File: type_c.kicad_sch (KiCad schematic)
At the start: 14 parts, among them U12 FUSB302B, U14 DPO2036

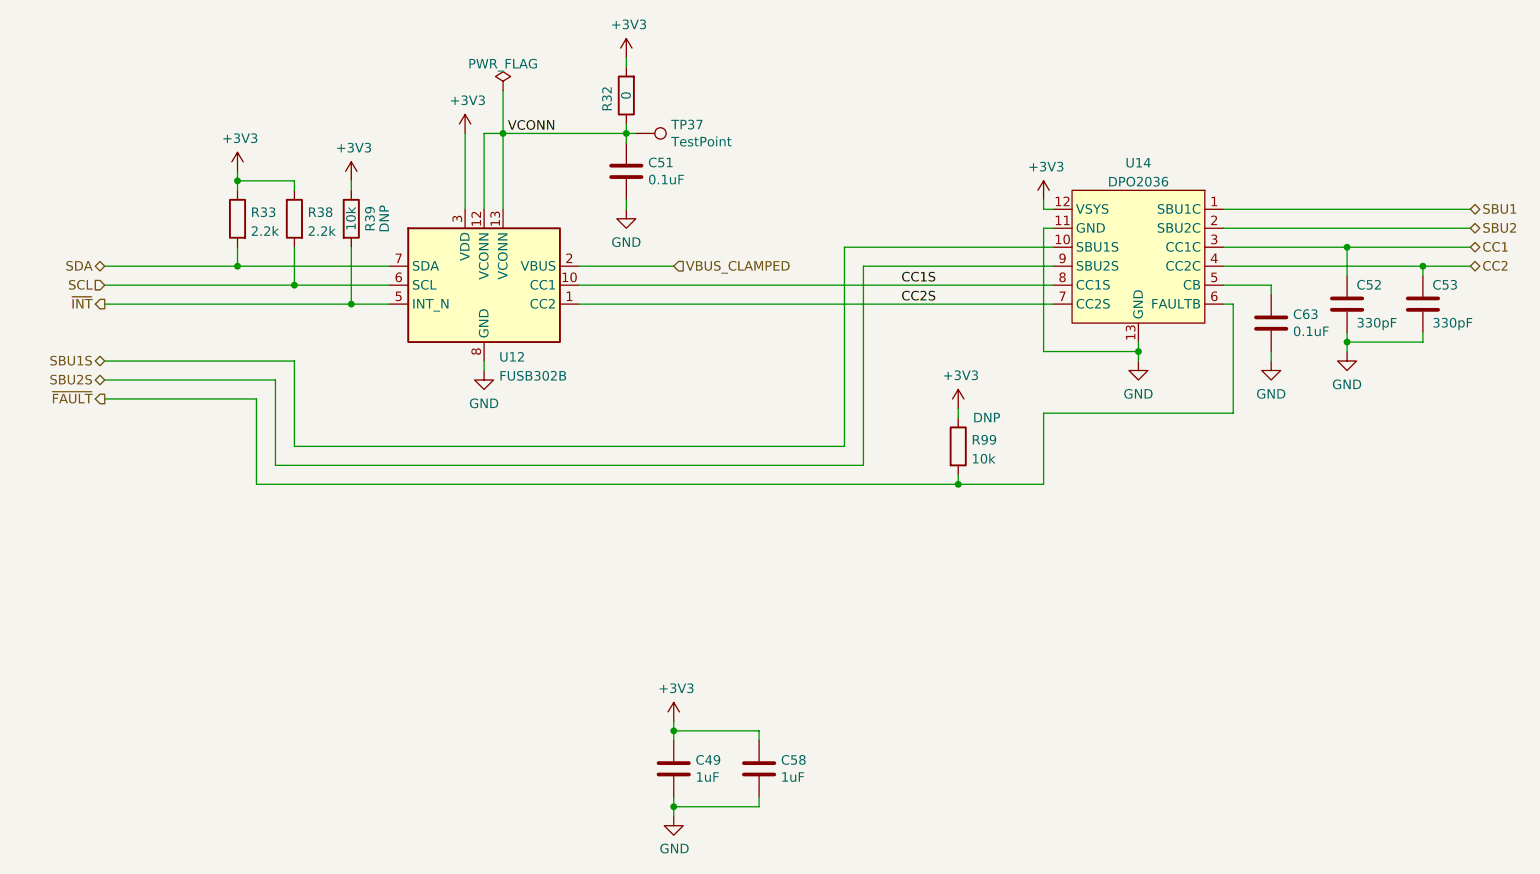
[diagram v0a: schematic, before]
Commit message: Upgrade to KiCad 7
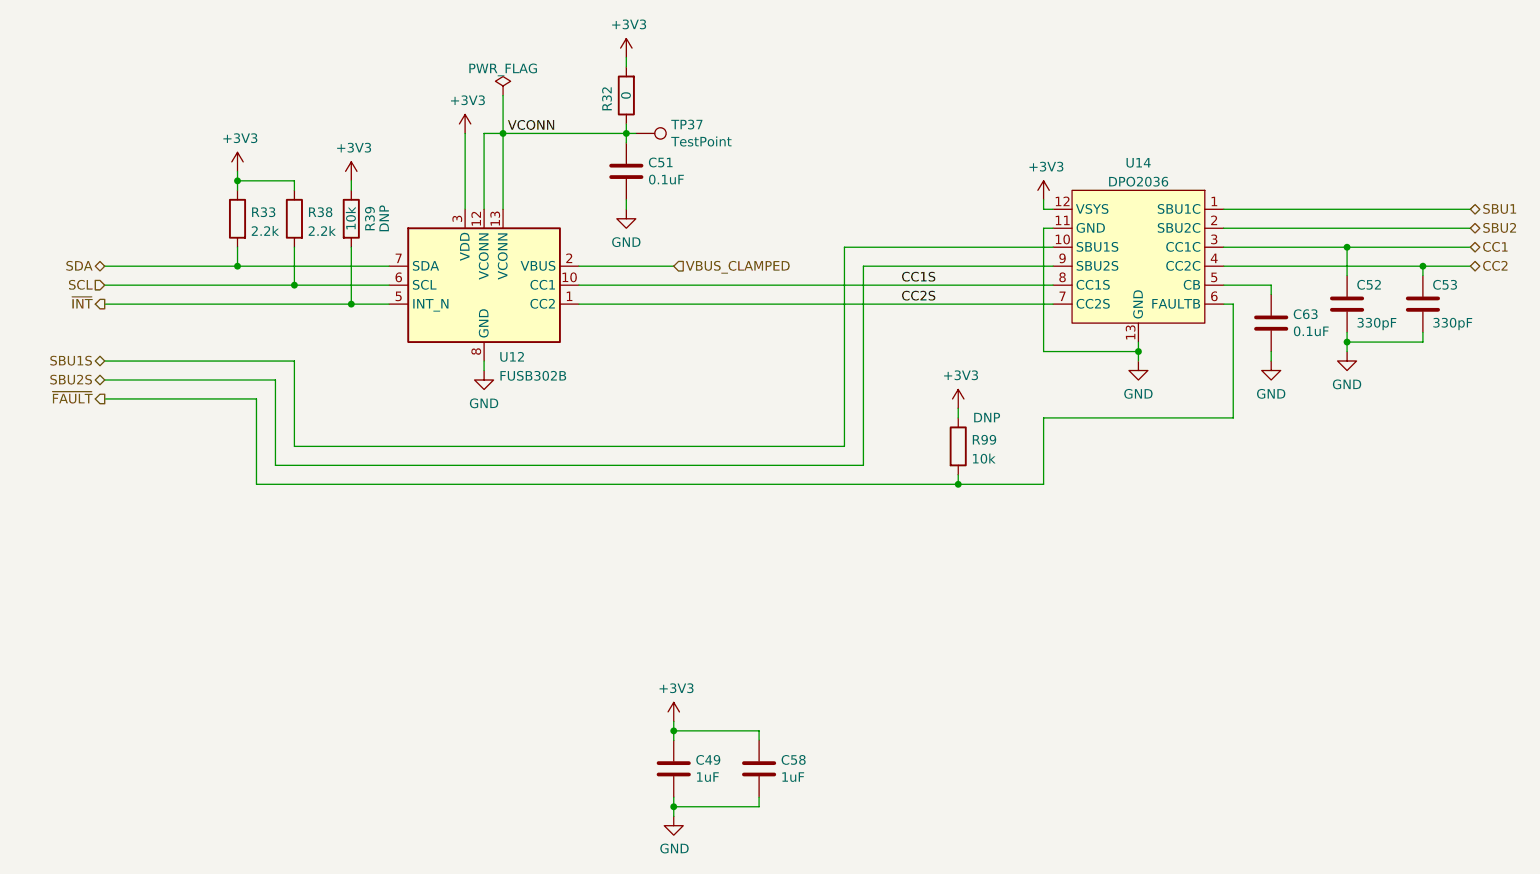
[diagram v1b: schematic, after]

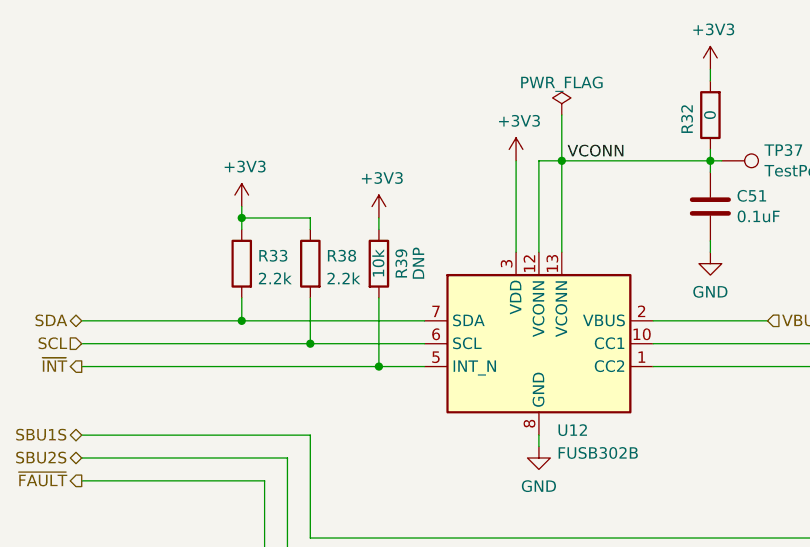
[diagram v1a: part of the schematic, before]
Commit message: Clean up schematic
- Renumber Pmod signal names to match silkscreen labels
- Clean up FPGA symbol
- Clean up PHY symbol
- Add title block to newer sheets
- Fix horizontal line in LED sheet
- Improve various label positions
- Update data sheet fields
- Renumber pages
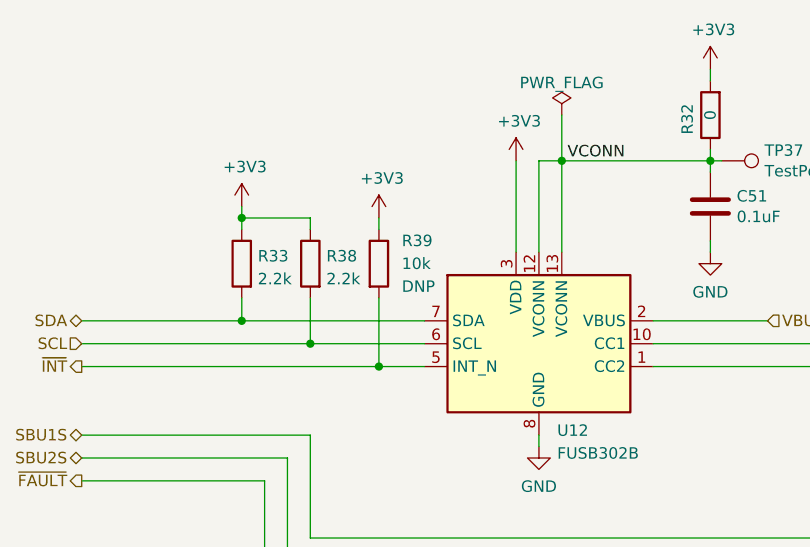
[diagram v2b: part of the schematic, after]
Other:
- company: (none) -> Copyright 2019-2023 Great Scott Gadgets
- title: (none) -> Cynthion
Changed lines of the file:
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@@
 (kicad_sch (version 20230121) (generator eeschema)
   (paper "A4")
+  (title_block
+    (title "Cynthion")
+    (date "${DATE}")
+    (rev "${VERSION}")
+    (company "Copyright 2019-2023 Great Scott Gadgets")
+    (comment 1 "Licensed under the CERN-OHL-P v2")
+  )
   (junction (at 127 152.4) (diameter 0) (color 0 0 0 0)
   )
@@
   )
   (symbol (lib_id "Device:R") (at 83.82 83.82 0) (unit 1)
-    (in_bom yes) (on_board yes) (dnp no)
-    (property "Reference" "R39" (at 86.36 83.82 90)
-      (effects (font (size 1.27 1.27)))
-    )
-    (property "Value" "10k" (at 83.82 83.82 90)
-      (effects (font (size 1.27 1.27)))
+    (in_bom yes) (on_board yes) (dnp no) (fields_autoplaced)
+    (property "Reference" "R39" (at 86.36 81.28 0)
+      (effects (font (size 1.27 1.27)) (justify left))
+    )
+    (property "Value" "10k" (at 86.36 83.82 0)
+      (effects (font (size 1.27 1.27)) (justify left))
     )
     (property "Footprint" "Resistor_SMD:R_0402_1005Metric" (at 82.042 83.82 90)
@@
       (effects (font (size 1.27 1.27)) hide)
     )
-    (property "DNP" "DNP" (at 88.265 83.82 90)
-      (effects (font (size 1.27 1.27)))
-    )
-    (pin "1")
+    (property "DNP" "DNP" (at 86.36 86.36 0)
+      (effects (font (size 1.27 1.27)) (justify left))
+    )
+    (pin "1")

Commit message: Update copyright notices
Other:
- company: Copyright 2019-2023 Great Scott Gadgets -> ${COPYRIGHT}
- title: Cynthion -> ${TITLE}
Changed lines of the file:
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@@
   (paper "A4")
   (title_block
-    (title "Cynthion")
+    (title "${TITLE}")
     (date "${DATE}")
     (rev "${VERSION}")
-    (company "Copyright 2019-2023 Great Scott Gadgets")
-    (comment 1 "Licensed under the CERN-OHL-P v2")
+    (company "${COPYRIGHT}")
+    (comment 1 "${LICENSE}")
   )
   (junction (at 127 152.4) (diameter 0) (color 0 0 0 0)
